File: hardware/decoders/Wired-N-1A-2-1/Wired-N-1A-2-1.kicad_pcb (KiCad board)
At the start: 2 copper layers, 9 x 20 mm, 37 parts, among them J1 CA, J10 RL, J11 RR, J12 FOF, J13 F0R, J14 MCLR, J15 +5, J16 GND, J17 PGD, J18 PGC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

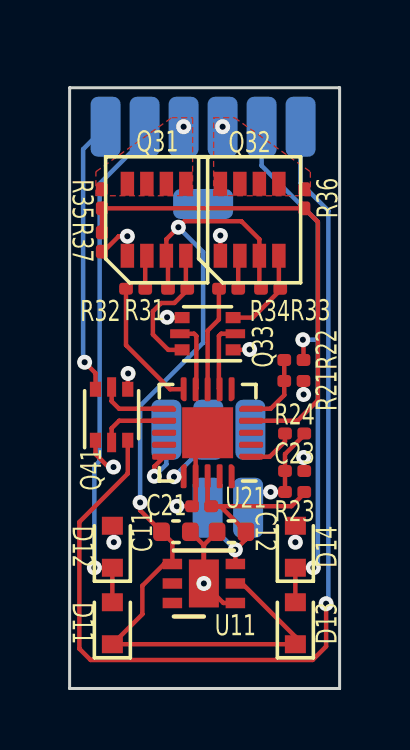
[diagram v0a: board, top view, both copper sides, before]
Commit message: Tweaked the board to shave 2mm, now 9mm x 18mm.
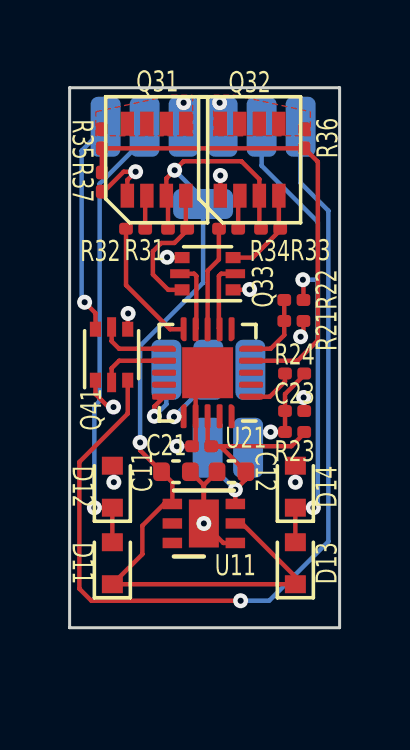
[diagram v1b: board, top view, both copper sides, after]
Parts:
- moved C11 2.00 mm to (53.5, 62.8)
- moved C12 2.00 mm to (55.4, 62.8)
- moved C21 2.00 mm to (54.4, 62.0)
- moved C23 2.00 mm to (57.5, 60.8)
- moved D11 2.00 mm to (51.4, 65.8)
- moved D12 2.00 mm to (51.4, 63.3)
- moved D13 2.00 mm to (57.5, 65.8)
- moved D14 2.00 mm to (57.5, 63.3)
- moved J14 2.00 mm to (56.0, 62.0)
- moved J15 2.00 mm to (54.6, 62.0)
- moved J16 2.00 mm to (56.0, 59.4)
- moved J17 2.00 mm to (54.6, 59.4)
- moved J18 2.00 mm to (53.2, 59.4)
- moved Q31 2.00 mm to (52.9, 52.4)
- moved Q32 2.00 mm to (56.0, 52.4)
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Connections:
- U11 pad 5: (no net) -> unconnected-(U11-Pad5)
- U11 pad 6: (no net) -> unconnected-(U11-Pad6)
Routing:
- net FOR_SP: track 33.9 -> 31.1 mm
- net RAIL_L: track 17.1 -> 15.1 mm
- net FOF_SP: track 9.23 -> 7.27 mm
- net GND: track 13.9 -> 15.3 mm
- net Vdrive: track 33.7 -> 32.5 mm
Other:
- board size 9 x 20 mm -> 9 x 18 mm
